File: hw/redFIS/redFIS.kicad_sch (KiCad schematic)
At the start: 59 parts, among them J1 USB_B, J2 DE9_Plug, J3 Conn_01x04, Q1 BC850, Q2 BC850, Q3 BC850, Q4 BC857, U1 ESP-32S, U2 AP63203WU, U3 AP63205WU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

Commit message: Changes in schematic
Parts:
- added C25: 10uF, symbol Device:C
- added C26: 470uF, symbol Device:C
- added D1: D, Diode_SMD:D_SMB_Handsoldering, symbol Device:D
- added J4: Conn_01x03, Connector_PinHeader_2.54mm:PinHeader_1x03_P2.54mm_Vertical, symbol Connector_Generic:Conn_01x03
- added R13: 10R, symbol Device:R
- added R14: 1R, symbol Device:R
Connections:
- net +12V: now also C26.1, D1.1 (K); no longer J2.9
- net +3.3VA: now also C25.1, R13.2
- net +3V3: now also R13.1
- net GND: now also C26.2, R14.1
- net GNDA: now also C25.2, J4.2 (Pin_2), R14.2
- net OUTL: now also J4.3 (Pin_3)
- net OUTR: now also J4.1 (Pin_1)
- new net: D1.2 (A), J2.9
- no-connect marks 5 -> 20

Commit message: Worked on HW design - layout
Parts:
- added C27: 10uF, Capacitor_SMD:C_0603_1608Metric_Pad1.08x0.95mm_HandSolder, symbol Device:C
- added C28: 100nF, Capacitor_SMD:C_0603_1608Metric_Pad1.08x0.95mm_HandSolder, symbol Device:C
- added C29, C30: 22uF, Capacitor_SMD:C_1210_3225Metric_Pad1.33x2.70mm_HandSolder, symbol Device:C_Polarized
- added L3: 3.9uH, Inductor_SMD:L_TracoPower_TCK-047_5.2x5.8mm, symbol Device:L
- added Rcan1: 120, Resistor_SMD:R_0603_1608Metric_Pad0.98x0.95mm_HandSolder, symbol Device:R
- added U7: AP63203WU, Package_TO_SOT_SMD:TSOT-23-6, symbol Regulator_Switching:AP63203WU
- C1, C10, C11, C12, C13, C15, C16, C17, C18, C19, C2, C20, C21, C22, C23, C24, C25, C4, C6, C9: footprint (none) -> Capacitor_SMD:C_0603_1608Metric_Pad1.08x0.95mm_HandSolder
- C14, C3, C5, C7, C8: footprint (none) -> Capacitor_SMD:C_1210_3225Metric_Pad1.33x2.70mm_HandSolder
- C26: footprint (none) -> Capacitor_THT:CP_Radial_D16.0mm_P7.50mm
- L1, L2: footprint (none) -> Inductor_SMD:L_TracoPower_TCK-047_5.2x5.8mm
- R1, R10, R11, R12, R2, R4, R6, R7, R8, R9, Rb1, Rb2: footprint (none) -> Resistor_SMD:R_0603_1608Metric_Pad0.98x0.95mm_HandSolder
- R13, R14: footprint (none) -> Resistor_SMD:R_1206_3216Metric_Pad1.30x1.75mm_HandSolder
- Ren1: renamed from Ren; footprint (none) -> Resistor_SMD:R_0603_1608Metric_Pad0.98x0.95mm_HandSolder
- Rl1: renamed from Rl; footprint (none) -> Resistor_SMD:R_0603_1608Metric_Pad0.98x0.95mm_HandSolder
- Rr1: renamed from Rr; footprint (none) -> Resistor_SMD:R_0603_1608Metric_Pad0.98x0.95mm_HandSolder
- Rstb1: renamed from Rstb; footprint (none) -> Resistor_SMD:R_0603_1608Metric_Pad0.98x0.95mm_HandSolder
- Rvio1: renamed from Rvio; footprint (none) -> Resistor_SMD:R_0603_1608Metric_Pad0.98x0.95mm_HandSolder
- U2: footprint Package_TO_SOT_SMD:TO-252-2 -> Package_TO_SOT_SMD:TSOT-23-6
- Y1: value Crystal_Small -> 12Mhz; footprint (none) -> Crystal:Crystal_SMD_HC49-SD_HandSoldering
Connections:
- net GNDA is gone; now on net GND: C16.2, C17.1, C18.2, C23.1, C24.1, C25.2, J4.2 (Pin_2), R14.2, U6.3 (CPGND), U6.9 (AGND)
- net +12V: now also C27.1, U7.2 (EN), U7.3 (IN)
- net +3.3VA: now also C29.1, C30.1, L3.1, U7.1 (FB)
- net +3V3: now also R7.1, R8.1
- net CANH: now also Rcan1.2
- net CANL: now also Rcan1.1
- net GND: now also C27.2, C29.2, C30.2, U7.4 (GND)
- net I2C_5V: no longer R7.1, R8.1
- new net: C28.2, L3.2, U7.5 (SW)
- new net: C28.1, U7.6 (BST)
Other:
- moved on the sheet: C1, C10, C11, C12, C13, C14, C25, C3, C4, C5, L1, R13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

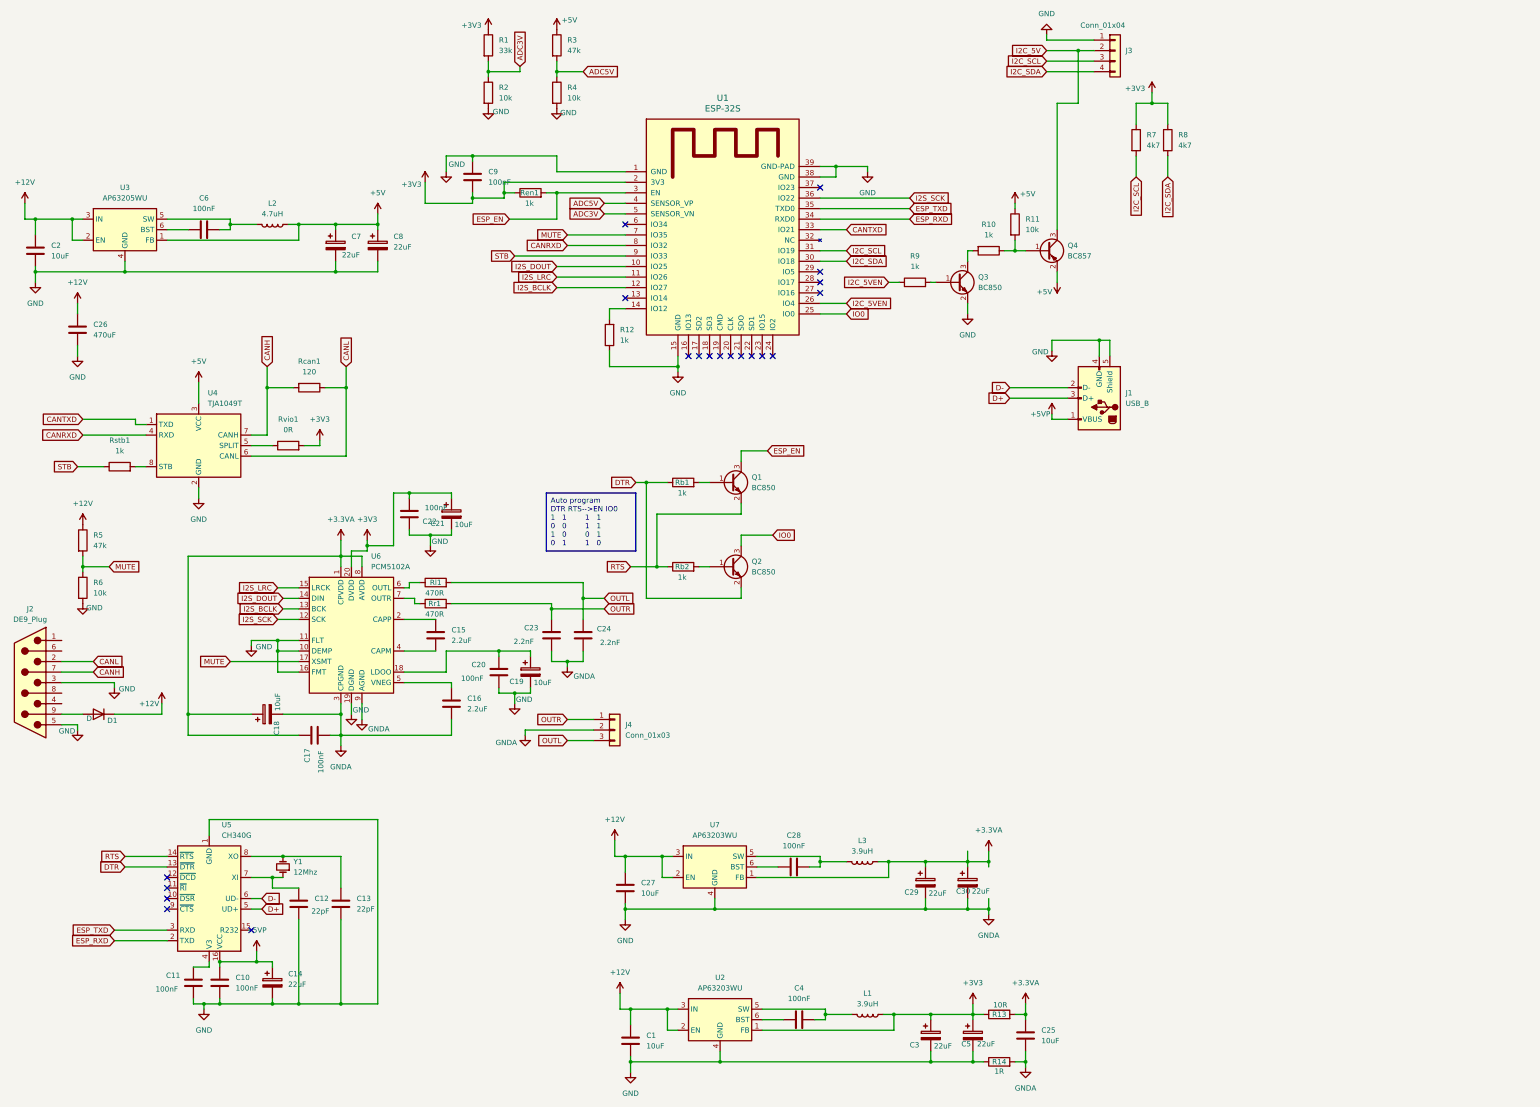
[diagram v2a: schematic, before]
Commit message: Finished first version of PCB
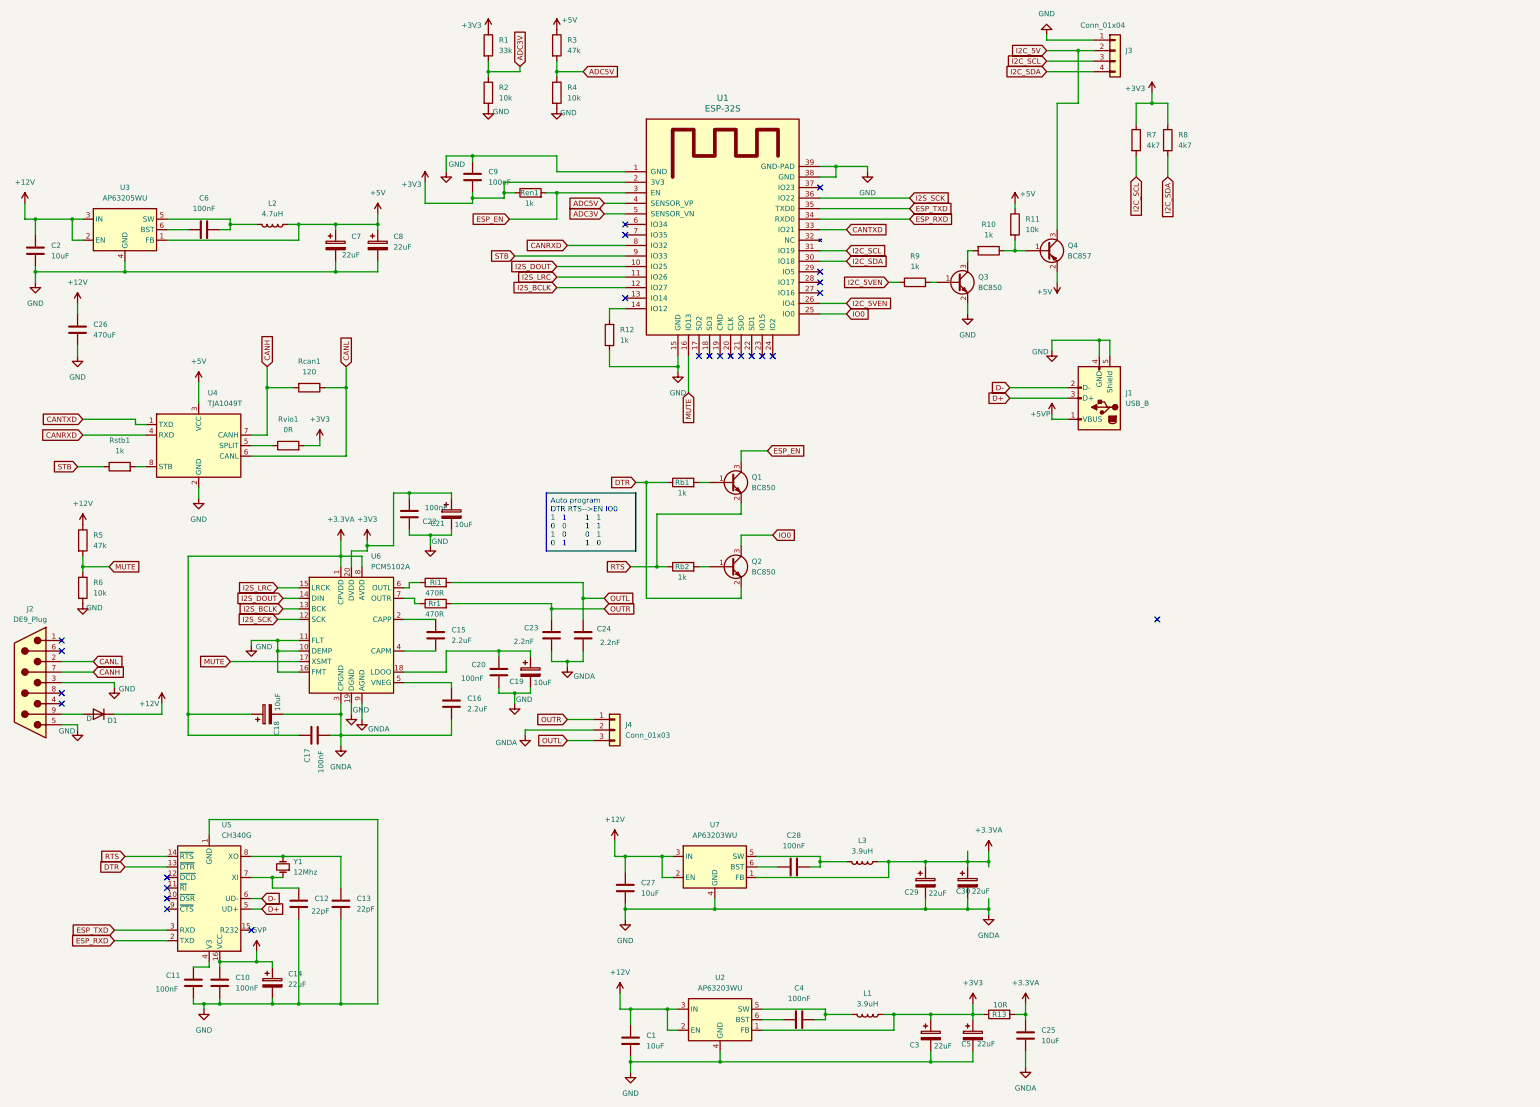
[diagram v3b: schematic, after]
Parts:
- removed R14: 1R, Resistor_SMD:R_1206_3216Metric_Pad1.30x1.75mm_HandSolder, symbol Device:R
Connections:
- net MUTE: now also U1.16 (IO13); no longer U1.7 (IO35)
- no-connect marks 20 -> 25
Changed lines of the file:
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@@
 	)
 	(junction
-		(at 246.38 266.7)
-		(diameter 0)
-		(color 0 0 0 0)
-	)
-	(junction
 		(at 77.47 222.25)
 		(diameter 0)
@@
 	)
 	(junction
-		(at 259.08 266.7)
-		(diameter 0)
-		(color 0 0 0 0)
-	)
-	(junction
 		(at 184.15 229.87)
 		(diameter 0)
@@
 	)
 	(no_connect
+		(at 26.67 177.8)
+	)
+	(no_connect
 		(at 209.55 81.28)
 	)
 	(no_connect
+		(at 290.83 160.02)
+	)
+	(no_connect
 		(at 198.12 96.52)
 	)
@@
 	)
 	(no_connect
-		(at 177.8 96.52)
+		(at 26.67 180.34)
 	)
 	(no_connect
@@
 	)
 	(no_connect
+		(at 26.67 167.64)
+	)
+	(no_connect
 		(at 52.07 229.87)
 	)
@@
 	)
 	(no_connect
+		(at 26.67 165.1)
+	)
+	(no_connect
 		(at 195.58 96.52)
 	)
 	(no_connect
+		(at 162.56 67.31)
+	)
+	(no_connect
 		(at 52.07 222.25)
 	)
@@
 	(wire
 		(pts
+			(xy 177.8 96.52) (xy 177.8 105.41)
+		)
+		(stroke
+			(width 0)
+			(type default)
+		)
+	)
+	(wire
+		(pts
 			(xy 78.74 165.1) (xy 78.74 167.64)
 		)
@@
 	(wire
 		(pts
-			(xy 259.08 266.7) (xy 259.08 267.97)
+			(xy 259.08 264.16) (xy 259.08 267.97)
 		)
 		(stroke
@@
 	(wire
 		(pts
-			(xy 259.08 264.16) (xy 259.08 266.7)
-		)
-		(stroke
-			(width 0)
-			(type default)
-		)
-	)
-	(wire
-		(pts
 			(xy 109.22 172.72) (xy 119.38 172.72)
 		)
@@
 	(wire
 		(pts
-			(xy 148.59 67.31) (xy 162.56 67.31)
-		)
-		(stroke
-			(width 0)
-			(type default)
-		)
-	)
-	(wire
-		(pts
 			(xy 99.06 180.34) (xy 99.06 184.15)
 		)
@@
 	(wire
 		(pts
-			(xy 246.38 266.7) (xy 248.92 266.7)
-		)
-		(stroke
-			(width 0)
-			(type default)
-		)
-	)
-	(wire
-		(pts
-			(xy 256.54 266.7) (xy 259.08 266.7)
-		)
-		(stroke
-			(width 0)
-			(type default)
-		)
-	)
-	(wire
-		(pts
 			(xy 57.15 187.96) (xy 83.82 187.96)
 		)
@@
 	(global_label "MUTE"
 		(shape input)
-		(at 148.59 67.31 180)
+		(at 177.8 105.41 270)
 		(fields_autoplaced yes)
 		(effects
@@
 		)
 		(property "Intersheetrefs" "${INTERSHEET_REFS}"
-			(at 140.7063 67.31 0)
+			(at 177.8 113.2937 90)
 			(effects
 				(font
@@
 					(unit 1)
 				)
-			)
-		)
-	)
-	(symbol
-		(lib_id "Device:R")
-		(at 252.73 266.7 90)
-		(unit 1)
-		(exclude_from_sim no)
-		(in_bom yes)
-		(on_board yes)
-		(dnp no)
-		(property "Reference" "R14"
-			(at 252.73 266.7 90)
-			(effects
-				(font
-					(size 1.27 1.27)
-				)
-			)
-		)
-		(property "Value" "1R"
-			(at 252.73 268.986 90)
-			(effects
-				(font
-					(size 1.27 1.27)
-				)
-			)
-		)
-		(property "Footprint" "Resistor_SMD:R_1206_3216Metric_Pad1.30x1.75mm_HandSolder"
-			(at 252.73 268.478 90)
-			(effects
-				(font
-					(size 1.27 1.27)
-				)
-				(hide yes)
-			)
-		)
-		(property "Datasheet" "~"
-			(at 252.73 266.7 0)
-			(effects
-				(font
-					(size 1.27 1.27)
-				)
-				(hide yes)
-			)
-		)
-		(property "Description" "Resistor"
-			(at 252.73 266.7 0)
-			(effects
-				(font
-					(size 1.27 1.27)
-				)
-				(hide yes)
-			)
-		)
-		(pin "2"
-		)
-		(pin "1"
-		)
-		(instances
-			(project "redFIS"
-				(path "/b70c9e0f-2e7b-47bd-a399-489f53f342f6"
-					(reference "R14")
-					(unit 1)
-				)

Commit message: HW design bugfix
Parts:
- added Q5: BC850, Package_TO_SOT_SMD:SOT-23, symbol Transistor_BJT:BC850
- added Q6: BC857, Package_TO_SOT_SMD:SOT-23, symbol Transistor_BJT:BC857
- added R14, R16, R17: 10k, Resistor_SMD:R_0603_1608Metric_Pad0.98x0.95mm_HandSolder, symbol Device:R
- added R15: 5k, Resistor_SMD:R_0603_1608Metric_Pad0.98x0.95mm_HandSolder, symbol Device:R
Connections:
- net +5V: now also Q6.2 (E), R16.1
- net CANRXD: now also R14.1, R15.1; no longer U4.4 (RXD)
- net CANTXD: now also R17.1; no longer U4.1 (TXD)
- net GND: now also Q5.2 (E), R14.2
- new net: Q5.1 (B), R17.2
- new net: Q5.3 (C), Q6.1 (B), R16.2
- new net: Q6.3 (C), U4.1 (TXD)
- new net: R15.2, U4.4 (RXD)
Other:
- moved on the sheet: Q3, Q4, R10, R11, R9, Rcan1, Rstb1, Rvio1, U4
